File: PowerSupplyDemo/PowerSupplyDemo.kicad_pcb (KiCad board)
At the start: 8 copper layers, 137 parts, among them J1 USB_C, Q1 BSZ060NE2LSATMA1, Q2 BSZ060NE2LSATMA1, SW1 219-3LPSTR, SW2 219-7LPSTR, SW3 219-2LPST, U2 TVS2200DRV, U3 TPS65988DJ, U4 LTC3833IUDC, U5 CP2102N-A01-GQFN28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

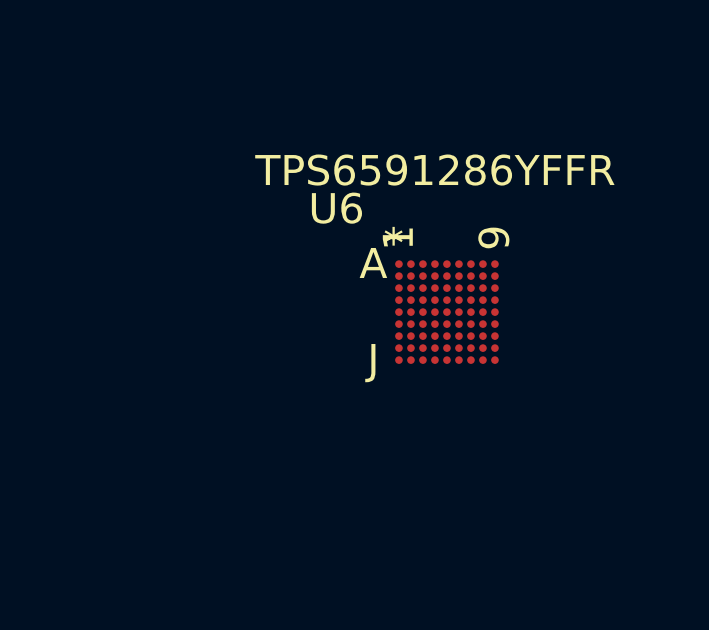
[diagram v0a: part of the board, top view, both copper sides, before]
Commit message: began laying out the tps
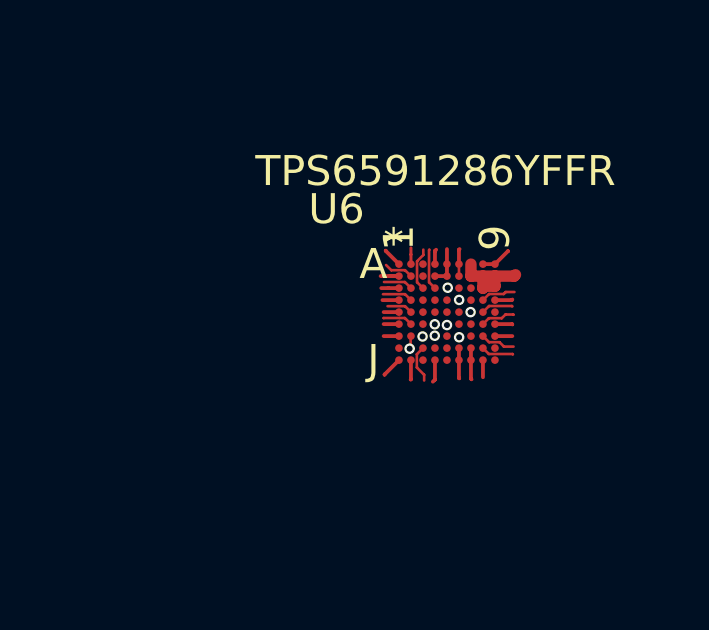
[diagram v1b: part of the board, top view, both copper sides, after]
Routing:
- net VSYS_3P3: track 0.00 -> 5.70 mm, vias 0 -> 1
- net GND: track 0.00 -> 1.86 mm
- net /PMIC/EN_LS0: track 0.00 -> 1.45 mm
- net Net-(R56-Pad1): track 0.00 -> 1.37 mm
- net Net-(C37-Pad1): track 0.00 -> 1.26 mm
- net Net-(C48-Pad1): track 0.00 -> 1.16 mm
- net /PMIC/EN2: track 0.00 -> 1.16 mm
- net Net-(C46-Pad1): track 0.00 -> 1.16 mm
- net Net-(C50-Pad1): track 0.00 -> 1.09 mm
- net /PMIC/EN1: track 0.00 -> 1.07 mm
- net VSYS_3P3_SDIO: track 0.00 -> 1.02 mm
- net /PMIC/config2: track 0.00 -> 1.01 mm
- net Net-(L2-Pad1): track 0.00 -> 1.01 mm
- net POS3P3_C0: track 0.00 -> 1.00 mm
- net /PMIC/EN_LS1: track 0.00 -> 0.98 mm
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
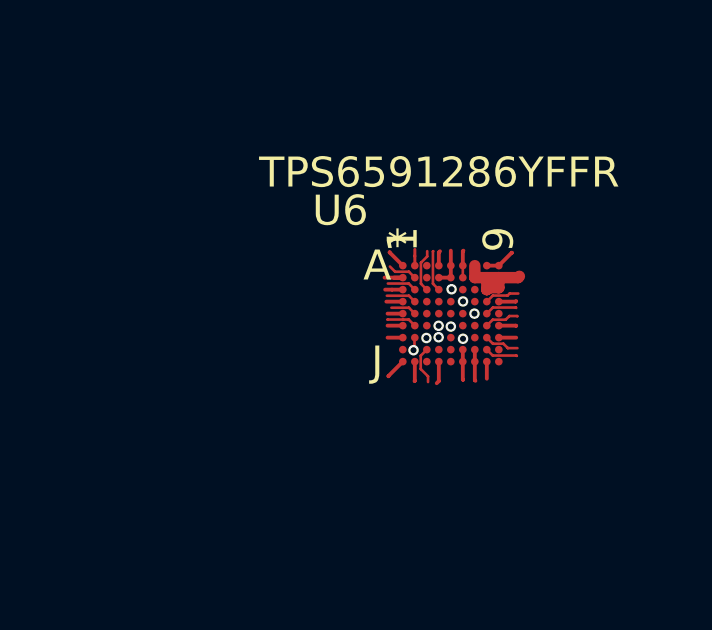
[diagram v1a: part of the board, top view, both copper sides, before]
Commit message: thickened outside fanout, and replaced inner levels with vip
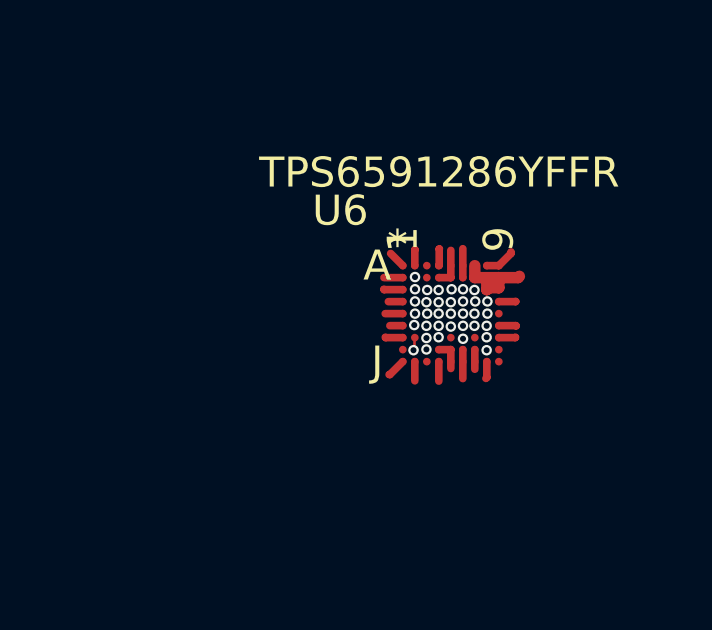
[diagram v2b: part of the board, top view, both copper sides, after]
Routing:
- net /PMIC/EN_LS0: track 1.45 -> 0.00 mm, vias 0 -> 1
- net Net-(R56-Pad1): track 1.37 -> 0.00 mm, vias 0 -> 1
- net GND: track 1.86 -> 3.13 mm, vias 0 -> 3
- net Net-(C37-Pad1): track 1.26 -> 0.00 mm, vias 0 -> 1
- net Net-(C48-Pad1): track 1.16 -> 0.00 mm, vias 0 -> 1
- net /PMIC/EN2: track 1.16 -> 0.00 mm, vias 0 -> 1
- net Net-(C46-Pad1): track 1.16 -> 0.00 mm, vias 0 -> 1
- net Net-(C50-Pad1): track 1.09 -> 0.00 mm, vias 0 -> 1
- net /PMIC/EN1: track 1.07 -> 0.00 mm, vias 0 -> 1
- net /PMIC/config2: track 1.01 -> 0.00 mm, vias 0 -> 1
- net POS3P3_C0: track 1.00 -> 0.00 mm, vias 0 -> 1
- net /PMIC/EN_LS1: track 0.98 -> 0.00 mm, vias 0 -> 1
- net Net-(D7-Pad1): track 0.98 -> 0.00 mm, vias 0 -> 1
- net /PMIC/config1: track 0.86 -> 0.00 mm, vias 0 -> 1
- net /PMIC/POS_1P8_IO: track 0.69 -> 0.64 mm, vias 0 -> 1
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
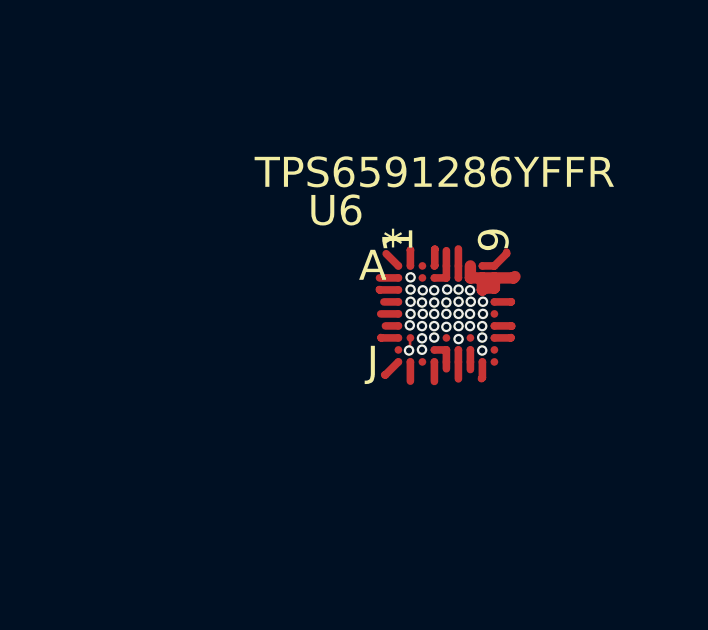
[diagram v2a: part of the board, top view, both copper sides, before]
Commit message: updated filled area parameters as well as trace widths for 0.4mm bga on pmic
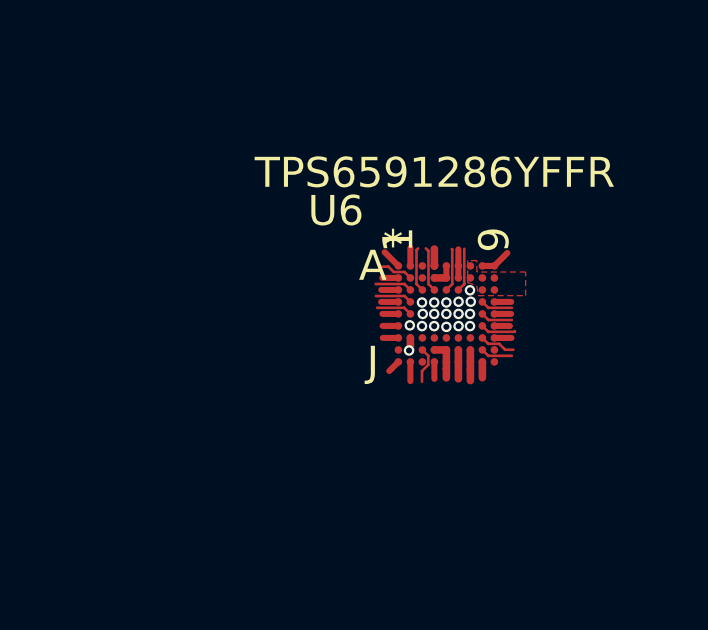
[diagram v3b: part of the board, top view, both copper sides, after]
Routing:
- net VSYS_3P3: track 5.36 -> 2.08 mm
- net Net-(R56-Pad1): track 0.00 -> 1.50 mm, vias 1 -> 0
- net /PMIC/EN_LS0: track 0.00 -> 1.49 mm, vias 1 -> 0
- net /PMIC/EN3: track 0.00 -> 1.45 mm, vias 1 -> 0
- net /PMIC/EN4: track 0.00 -> 1.45 mm, vias 1 -> 0
- net /PMIC/EN_LS1: track 0.00 -> 1.24 mm, vias 1 -> 0
- net /PMIC/config2: track 0.00 -> 1.23 mm, vias 1 -> 0
- net Net-(C37-Pad1): track 0.00 -> 1.23 mm, vias 1 -> 0
- net Net-(C48-Pad1): track 0.00 -> 1.20 mm, vias 1 -> 0
- net /PMIC/config1: track 0.00 -> 1.20 mm, vias 1 -> 0
- net Net-(C46-Pad1): track 0.00 -> 1.17 mm, vias 1 -> 0
- net Net-(D7-Pad1): track 0.00 -> 1.09 mm, vias 1 -> 0
- net /PMIC/EN1: track 0.00 -> 1.07 mm, vias 1 -> 0
- net Net-(C50-Pad1): track 0.00 -> 1.07 mm, vias 1 -> 0
- net /PMIC/EN2: track 0.00 -> 1.07 mm, vias 1 -> 0
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- added copper zone on In1.Cu, net GND
- added copper zone on F.Cu, net VSYS_3P3

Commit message: updated constraints again.
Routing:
- net I2C0_SCL_C0: track 0.00 -> 2.72 mm
- net I2C0_SDA_C0: track 0.00 -> 2.37 mm
- net DCD1_PWM_AVS: track 0.00 -> 2.06 mm
- net DCD1_CLK_AVS: track 0.00 -> 1.96 mm
- net WATCHDOG_CLOCK_OUT: track 0.00 -> 1.96 mm
- net SPI0_D1_C0: track 0.00 -> 1.87 mm
- net SPI0_CLK_C0: track 0.00 -> 1.86 mm
- net SPI0_D0_C0: track 0.00 -> 1.85 mm
- net PMIC_ENABLE: track 0.00 -> 1.79 mm
- net /PMIC/LDOA: track 0.00 -> 1.78 mm
- net /PMIC/POS_1P8_IO: track 0.43 -> 1.92 mm
- net /PMIC/iic_or_spi_cntrl: track 0.00 -> 1.40 mm
- net POS1P8_C0: track 0.00 -> 1.35 mm
- net POS3P3_C0: track 0.00 -> 1.02 mm
- net VSYS_3P3: track 2.08 -> 2.47 mm, vias 1 -> 3
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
